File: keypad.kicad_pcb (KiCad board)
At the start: 2 copper layers, 76.3 x 115.3 mm, 79 parts, among them J1 Conn_01x04_Female, J3 USB_C_Receptacle_USB2.0, K1_1 KEYSW, K1_2 KEYSW, K1_3 KEYSW, K1_4 KEYSW, K2_1 KEYSW, K2_2 KEYSW, K2_3 KEYSW, K2_4 KEYSW, K3_1 KEYSW, K3_2 KEYSW, K3_3 KEYSW, K3_4 KEYSW, K4_1 KEYSW, K4_2 KEYSW, K4_3 KEYSW, K4_4 KEYSW, K5_1 KEYSW, K5_2 KEYSW, K5_3 KEYSW, Q1 BC847, SW1 SW_Push, U1 STM32F303C6Tx, U2 MCP1804x-3302xOT, Y1 A7 8MHz

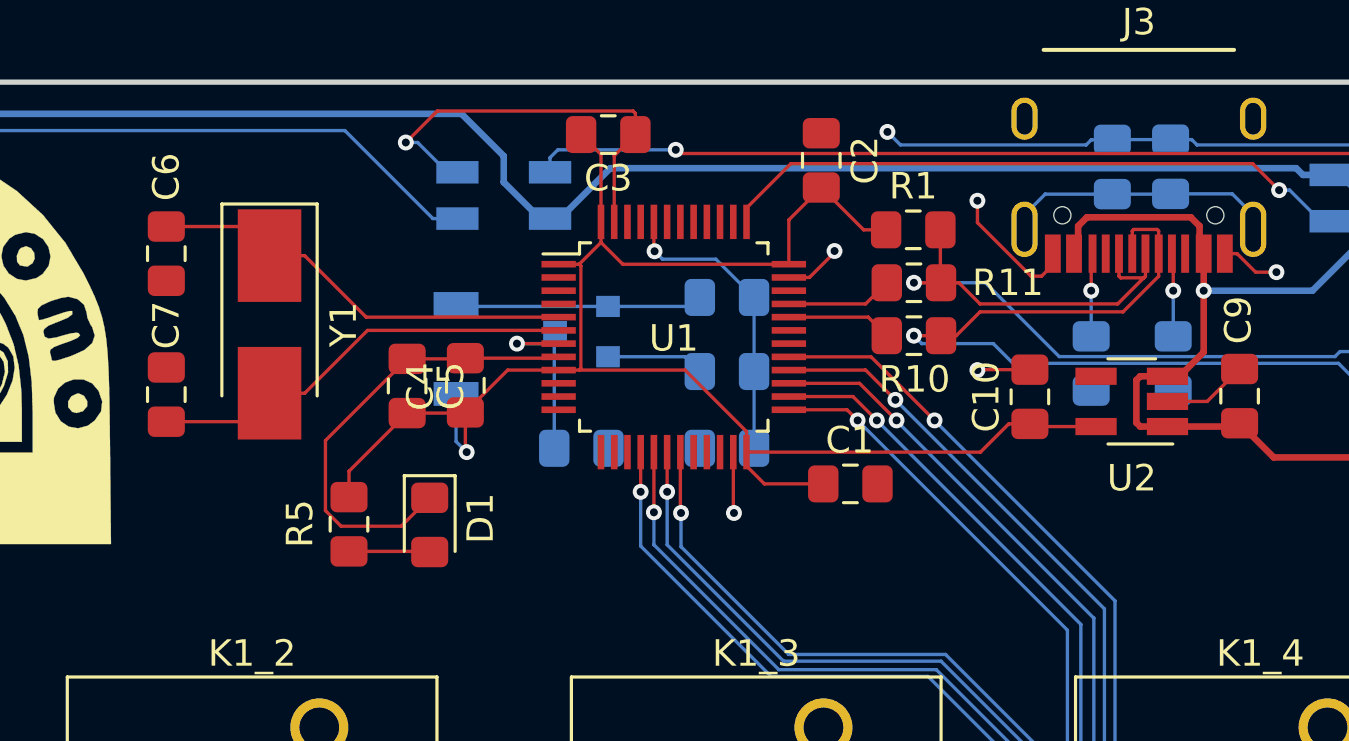
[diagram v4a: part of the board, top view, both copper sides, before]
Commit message: - Quarz geaendert - Debug LED hinzugefügt
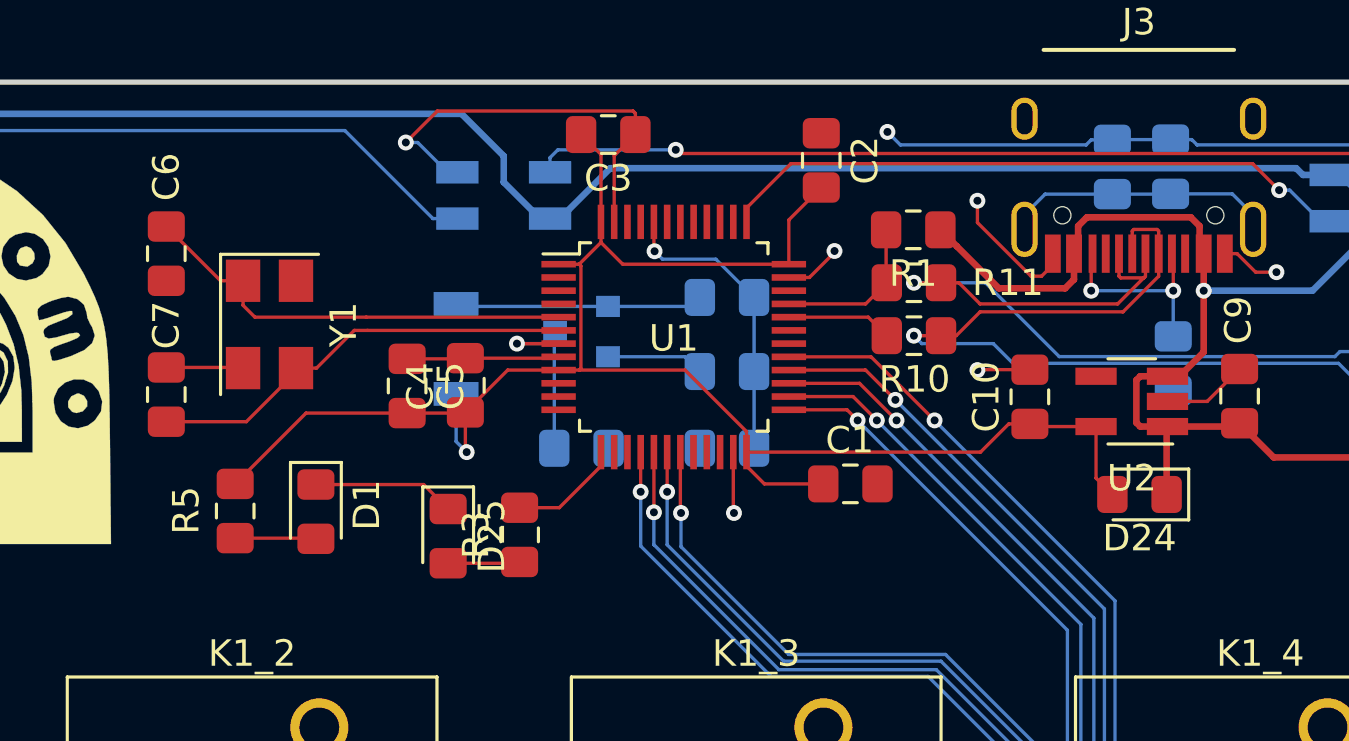
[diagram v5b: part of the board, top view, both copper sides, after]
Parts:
- removed R8: 5.1k, Resistor_SMD:R_0805_2012Metric_Pad1.15x1.40mm_HandSolder
- added D24: 1N4148, Diode_SMD:D_0805_2012Metric_Pad1.15x1.40mm_HandSolder, F.Cu at (170.7, 51.3)
- added D25: POWER_LED, LED_SMD:LED_0805_2012Metric_Pad1.15x1.40mm_HandSolder, F.Cu at (144.6, 52.9)
- added R3: 330, Resistor_SMD:R_0805_2012Metric_Pad1.15x1.40mm_HandSolder, F.Cu at (147.3, 52.8)
- C1, C2, C3: value 0.1u -> 100n
- C12, C8: value 4.7u -> 4.7n
- C4: value 0.1u -> 1u
- C6, C7: value 18p -> 22p
- Y1: footprint Crystal:Crystal_SMD_5032-2Pin_5.0x3.2mm_HandSoldering -> Crystal:Crystal_SMD_5032-4Pin_5.0x3.2mm
- moved D1 4.33 mm to (139.6, 52.0)
- moved R5 4.33 mm to (136.6, 51.9)
- turned R1 to 180 degrees
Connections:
- J3 pad B5: Net-(J3-PadB5) -> Net-(J3-PadA5)
- R1 pad 1: +3V3 -> VBUS
- R1 pad 2: USB_P -> Net-(R1-Pad2)
- R11 pad 1: Net-(R11-Pad1) -> Net-(R1-Pad2)
- U1 pad 13: (no net) -> Net-(R3-Pad2)
- U1 pad 33: Net-(R11-Pad1) -> Net-(R1-Pad2)
- Y1 pad 2: OSC_OUT -> GND
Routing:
- net VBUS: track 370.1 -> 379.8 mm
- net Net-(R1-Pad2): track 0.00 -> 6.04 mm
- net Net-(J3-PadA5): track 3.15 -> 7.67 mm, vias 1 -> 2
- net Net-(R3-Pad2): track 0.00 -> 4.29 mm
- net Net-(R11-Pad1): track 4.03 -> 0.00 mm
- net GND: track 89.7 -> 86.4 mm
- net +3V3: track 64.9 -> 68.2 mm
- net Net-(J3-PadB5): track 3.15 -> 0.00 mm, vias 1 -> 0
- net Net-(D25-Pad2): track 0.00 -> 2.79 mm
- net USB_P: track 33.2 -> 31.3 mm
- net OSC_IN: track 16.2 -> 16.8 mm
